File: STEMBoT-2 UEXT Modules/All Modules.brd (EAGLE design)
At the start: 81.2 x 50.7 mm, 39 parts, among them IC3 8to3 Encoder, IC6 8to3 Encoder, U1 HC-SR04, U2 TESEO-LIV3F, U3 CYBLE-012011-00

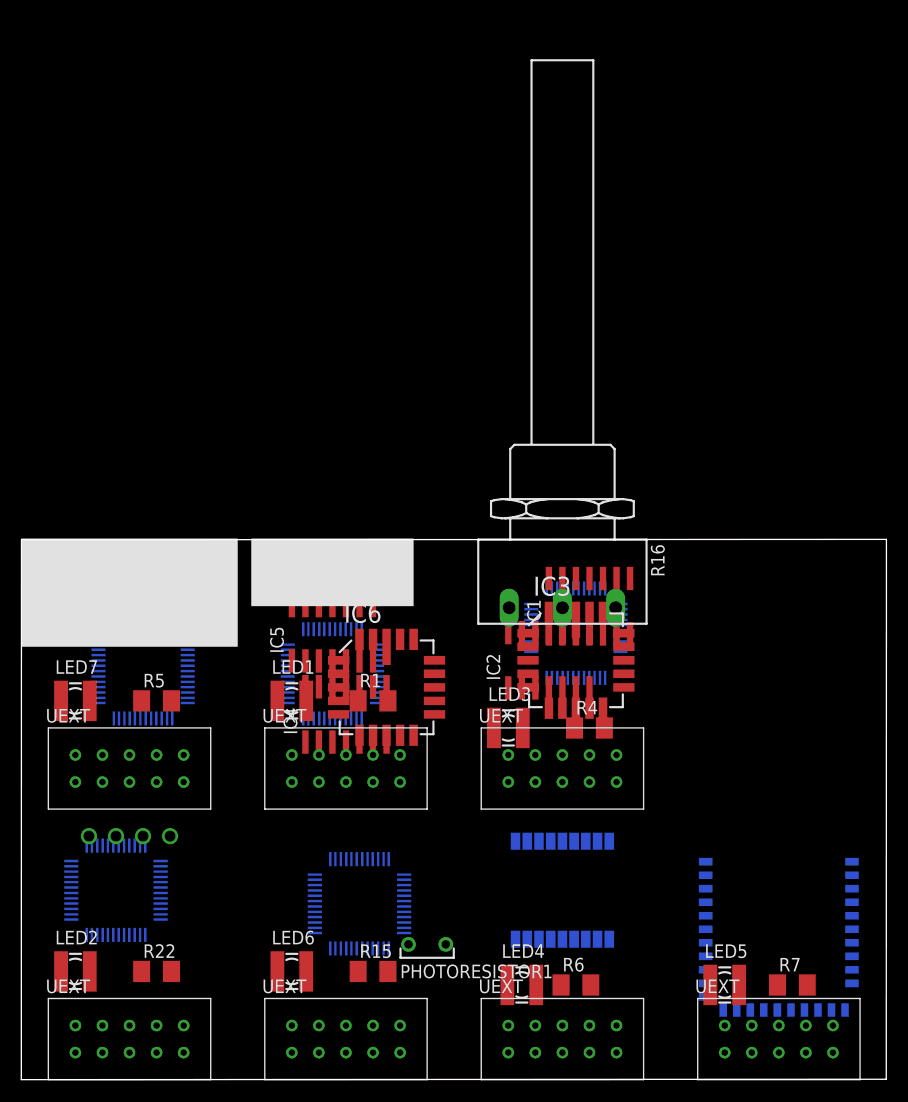
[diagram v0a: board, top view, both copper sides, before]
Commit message: changes to pcb with 6 mil traces
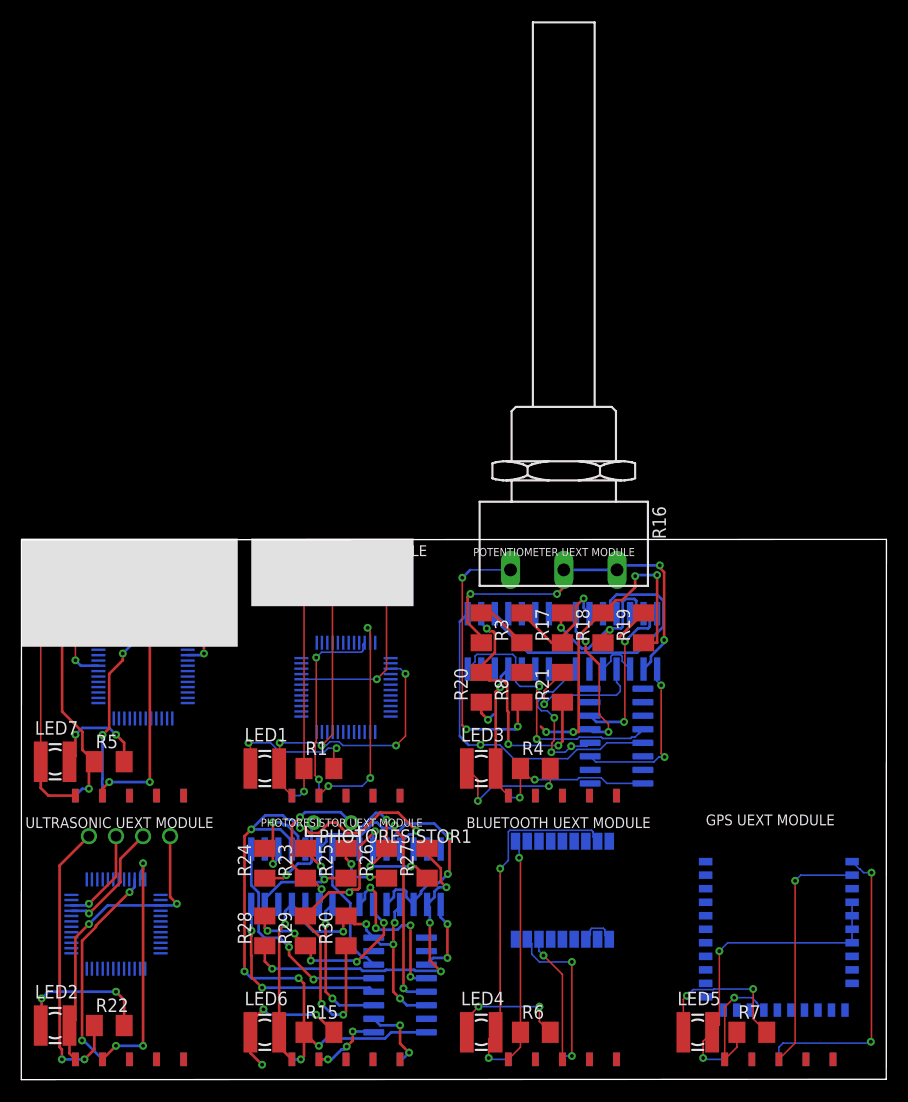
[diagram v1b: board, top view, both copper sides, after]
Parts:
- removed IC3, IC6: 8to3 Encoder, 74xx-eu:LCC20
- removed UX1, UX2, UX3, UX4, UX5, UX8, UX9: UEXT-CON, UEXT-Connecotr:UEXT-CON
- added R17, R18, R19, R2, R20, R21, R23, R24, R25, R26, R27, R28, R29, R3, R30, R8: 10k, rcl:M1206
- added U$12, U$2, U$3, U$7, U$8: UEXT-SMD, UEXT-Connecotr:UEXT-SMD
- added U$13, U$14: PARALLEL2SERIAL, SOIC127P600X175-16N:SOIC127P600X175-16N
- U$5, U$9: value LPC11C24FBD48/301 -> UEXT-SMD; device QFP50P900X900X160-48N:QFP50P900X900X160-48N -> UEXT-Connecotr:UEXT-SMD
- moved U$5 44.6 mm to (10.2, 26.7), flipped to the top
- moved U$9 24.0 mm to (50.8, 1.91), flipped to the top
- moved IC5 23.7 mm to (35.6, 19.1), flipped to the bottom
- moved IC4 16.1 mm to (25.4, 19.1), flipped to the bottom
- moved PHOTORESISTOR1 14.5 mm to (29.2, 24.1)
- moved R1 8.13 mm to (27.9, 29.2)
- moved R15 7.65 mm to (27.9, 4.45)
- moved R5 7.24 mm to (8.26, 29.8)
- moved LED1 6.84 mm to (22.9, 29.2)
- moved R22 6.75 mm to (8.26, 5.08)
- moved R4 6.35 mm to (48.3, 29.2)
- moved LED6 6.25 mm to (22.9, 4.45)
- moved LED7 6.02 mm to (3.17, 29.8)
- moved LED4 5.85 mm to (43.2, 4.45)
- moved R6 5.85 mm to (48.3, 4.45)
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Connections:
- removed net GND: IC3.10, IC6.10
- removed net N$46: IC3.9, U$5.34
- removed net N$47: IC3.8, U$5.35
- removed net N$70: U$9.46, UX8.3
- removed net N$71: U$9.47, UX8.4
- removed net N$72: IC6.12, U$9.33
- removed net N$73: IC6.9, U$9.34
- removed net N$74: IC6.8, U$9.35
- removed net V+: IC1.4, IC2.4, IC4.4, IC5.4
- removed net V-: IC1.11, IC2.11, IC4.11, IC5.11
- removed net VCC: IC3.20, IC6.20
- new net N$18: PHOTORESISTOR1.1, R24.1
- new net N$20: R16.1E, R8.1
- net N$1: now also U$8.1; no longer UX2.1
- net N$10: now also IC1.4, IC2.4, R21.2, U$13.16, U$13.6, U$2.2; no longer IC3.5, IC3.7, U$5.21, U$5.3, UX1.2
- net N$11: now also U$13.10, U$2.9; no longer U$5.47, UX1.4
- net N$12: now also U$14.9, U$3.4; no longer IC3.12, U$5.33
- net N$14: now also U$5.2; no longer UX3.2
- net N$15: now also U$5.3; no longer UX3.3
- net N$16: now also U$5.4; no longer UX3.4
- net N$19: now also U$14.10, U$3.9; no longer U$9.3
- net N$21: now also U$9.2; no longer UX5.2
- net N$22: now also U$9.1; no longer UX5.1
- net N$23: now also U$9.5; no longer UX5.5
- net N$24: now also U$9.6; no longer UX5.6
- net N$26: now also U$12.1; no longer UX4.1
- net N$27: now also U$12.6; no longer UX4.6
- net N$28: now also U$12.5; no longer UX4.5
- net N$29: now also U$12.2; no longer UX4.2
- net N$3: now also U$8.2; no longer UX2.2
- net N$33: now also R2.2, R3.1
- net N$34: now also R17.1, R3.2
- net N$35: now also R17.2, R18.1
- net N$36: now also R18.2, R19.1
- net N$37: now also R19.2, R20.1
- net N$38: now also R20.2, R21.1
- net N$39: now also U$13.11; no longer IC3.13
- net N$4: now also U$8.3; no longer UX2.3
- net N$40: now also U$13.12; no longer IC3.14
- net N$41: now also U$13.13; no longer IC3.15
- net N$42: now also U$13.14; no longer IC3.17
- net N$43: now also U$13.3; no longer IC3.2
- net N$44: now also U$13.4; no longer IC3.3
- net N$45: now also U$13.5; no longer IC3.4
- net N$48: now also R8.2; no longer R16.1E
- net N$49: now also R25.2, R26.1
- net N$5: now also U$8.4; no longer UX2.4
- net N$50: now also R2.1
- net N$52: now also IC1.11, IC2.11, U$13.8, U$2.1; no longer U$5.20, UX1.1
- net N$54: now also R26.2, R27.1
- net N$55: now also R27.2, R28.1
- net N$56: now also R28.2, R29.1
- net N$57: now also R29.2, R30.1
- net N$58: now also U$14.11; no longer IC6.13
- net N$59: now also U$14.12; no longer IC6.14
- net N$60: now also U$14.13; no longer IC6.15
- net N$61: now also U$14.14; no longer IC6.17
- net N$62: now also U$14.3; no longer IC6.2
- net N$63: now also U$14.4; no longer IC6.3
- net N$64: now also U$14.5; no longer IC6.4
- net N$65: now also R24.2; no longer PHOTORESISTOR1.1
- net N$66: now also IC4.11, IC5.11, U$14.8, U$3.1; no longer U$9.20, UX8.1
- net N$68: now also R23.1
- net N$69: now also IC4.4, IC5.4, R30.2, U$14.16, U$14.6, U$3.2; no longer IC6.5, IC6.7, U$9.21, UX8.2
- net N$7: now also U$5.1; no longer UX3.1
- net N$8: now also U$13.9, U$2.4; no longer U$5.46, UX1.3
- net N$81: now also U$7.1; no longer UX9.1
- net N$84: now also U$7.2; no longer UX9.2
- net N$85: now also U$7.3; no longer UX9.3
- net N$86: now also U$7.4; no longer UX9.4
- net N$9: now also R23.2, R25.1
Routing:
- net N$66: track 0.00 -> 66.9 mm, vias 0 -> 7
- net N$69: track 0.00 -> 41.7 mm, vias 0 -> 6
- net N$3: track 0.00 -> 41.5 mm, vias 0 -> 4
- net N$14: track 0.00 -> 38.6 mm, vias 0 -> 3
- net N$50: track 0.00 -> 35.8 mm, vias 0 -> 4
- net N$22: track 0.00 -> 33.0 mm, vias 0 -> 2
- net N$55: track 0.00 -> 32.5 mm, vias 0 -> 4
- net N$48: track 0.00 -> 32.2 mm
- net N$57: track 0.00 -> 31.7 mm, vias 0 -> 4
- net N$65: track 0.00 -> 30.8 mm, vias 0 -> 4
- net N$36: track 0.00 -> 30.8 mm, vias 0 -> 4
- net N$45: track 0.00 -> 30.5 mm, vias 0 -> 1
- net N$26: track 0.00 -> 29.3 mm, vias 0 -> 2
- net N$84: track 0.00 -> 29.3 mm, vias 0 -> 2
- net N$28: track 0.00 -> 28.1 mm, vias 0 -> 2
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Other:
- board text added: "BLUETOOTH UEXT MODULE"
- board text added: "GPS UEXT MODULE"
- board text added: "IR REMOTE UEXT MODULE"
- board text added: "IR SESNOR UEXT MODULE"
- board text added: "PHOTORESISTOR UEXT MODULE"
- board text added: "POTENTIOMETER UEXT MODULE"
- board text added: "ULTRASONIC UEXT MODULE"

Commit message: added board file and new switch library
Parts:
- removed IC4, IC5: (no value), linear:SO14
- removed PHOTORESISTOR1: M9960_11A, photo-elements:M9960
- added C1, C10, C2, C3, C4, C5, C6, C7, C8, C9: CAPACITORS-0603, CAPACITORS:C0603
- added D1, D3: SFH482, led:SFH482
- added D2, D4: BP104, opto-trans-siemens:BP104
- added DZ1, DZ2: LZR182, led:LZR182
- added IC3: 74HC165PW,118, 74HC165PW_118:SOP65P640X110-16N
- added J1, J2, J3, J4, J5, J6: FTSH-105-01-XXX-DV-K, FTSH-105-01-XXX-DV-K:FTSH-105-01-XXX-DV-K
- added LED8: LSG-T676, led:P-LCC4-0
- added PH1, PH2: VT20N1, photo-elements:TO46-VT200
- added Q1: MMBT3904LP-7, NPN BJT:DFN101X61X53-3N
- added Q2, Q3: MMBT3904LP-7, MMBT3904LP-7:DFN101X61X53-3N
- added R10, R11, R12, R13, R14, R31, R32, R33, R34, R35, R36, R37, R38, R39, R40, R41, R42, R49, R50, R51, R55, R61, R9: ERJ-1RHD3601C, Resistor:RESC0603X26N
- added R43, R44, R45, R46, R47, R48, R52, R53, R57, R58: 1k, rcl:M1206
- added R54: PC16S, piher:PC16S
- added S1, S2, S3, S4, S5, S6: 2-1437565-7, 2-1437565-7 (tactile switch):SW_2-1437565-7
- added U$15: UEXT-SMD, UEXT-Connecotr:UEXT-SMD
- added U10, U4, U7: SN74HC148D, SN74HC148D:SOIC127P600X175-16N
- added U11, U12, U5, U6, U8, U9: MAX964ESET, MAX964ESET:SOIC127P600X175-16N
- added U13: HC-SR04, HC-SR04:XCVR_HC-SR04
- added VR1, VR2: PVG3A200C01R00, TrimmerPot:TRIM_PVG3A200C01R00
- IC1, IC2: value (none) -> 74HC165PW,118; device linear:SO14 -> 74HC165PW_118:SOP65P640X110-16N
- R1, R15, R4, R5: value 1k -> ERJ-1RHD3601C; device rcl:M1206 -> Resistor:RESC0603X26N
- R16: value 1K ohm -> ERJ-1RHD3601C; device piher:PC16S -> Resistor:RESC0603X26N
- R17, R18, R19, R2, R21, R23, R24, R25, R26, R27, R28, R29, R3, R30, R8: value 10k -> ERJ-1RHD3601C; device rcl:M1206 -> Resistor:RESC0603X26N
- R20: value 10k -> PC16S; device rcl:M1206 -> piher:PC16S
- U$1, U$10: value LPC11C24FBD48/301 -> UEXT-SMD; device QFP50P900X900X160-48N:QFP50P900X900X160-48N -> UEXT-Connecotr:UEXT-SMD
- U$11: value CHQ1838 -> LPC11C24FBD48/301; device IRSensors:CHQ1838 -> QFP50P900X900X160-48N:QFP50P900X900X160-48N
- U$13: value PARALLEL2SERIAL -> UEXT-SMD; device SOIC127P600X175-16N:SOIC127P600X175-16N -> UEXT-Connecotr:UEXT-SMD
- U$14: value PARALLEL2SERIAL -> LPC11C24FBD48/301; device SOIC127P600X175-16N:SOIC127P600X175-16N -> QFP50P900X900X160-48N:QFP50P900X900X160-48N
- U$4: value HW740 -> LPC11C24FBD48/301; device IRSensors:HW740 -> QFP50P900X900X160-48N:QFP50P900X900X160-48N
- U$7: value UEXT-SMD -> LPC11C24FBD48/301; device UEXT-Connecotr:UEXT-SMD -> QFP50P900X900X160-48N:QFP50P900X900X160-48N
- U1: value HC-SR04 -> TSL260R-LF; device HC-SR04:XCVR_HC-SR04 -> TSL260R-LF:XDCR_TSL260R-LF
- moved R4 718.5 mm to (-334.0, 637.5)
- moved R8 718.2 mm to (-346.7, 637.5), turned to 0 degrees
- moved R3 703.2 mm to (-327.7, 637.5), turned to 0 degrees
- moved R5 700.6 mm to (-340.4, 637.5)
- moved R1 698.3 mm to (-315.0, 637.5)
- moved R2 697.9 mm to (-321.3, 637.5), turned to 0 degrees
- moved R7 691.1 mm to (-205.7, 638.8)
- moved IC2 684.0 mm to (-287.0, 638.8), flipped to the top
- moved IC1 681.6 mm to (-271.8, 638.8), flipped to the top
- moved R6 681.5 mm to (-200.7, 638.8)
- moved R22 670.5 mm to (-210.8, 638.8)
- moved LED5 657.4 mm to (-104.1, 640.1)
- moved R30 651.2 mm to (-119.4, 647.7), turned to 0 degrees
- moved LED6 650.5 mm to (-115.6, 640.1)
- moved U1 650.2 mm to (-194.3, 640.1), flipped to the top, turned to 0 degrees
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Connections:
- removed net GND_RF: U2.10, U2.12
- removed net N$3 (its old number): LED1.A, U$11.P$2, U$6.3, U$8.2
- removed net VCC_IO: U2.7
- removed net VCC_RF: U2.14
- removed net VDDR: U3.29
- new net N$100: U4.1, U6.15
- new net N$101: U4.12, U6.14
- new net N$102: U4.11, U6.11
- new net N$103: U4.10, U6.10
- new net N$104: U10.10, U12.10
- new net N$105: R1.2, R42.1, U11.1
- new net N$106: IC2.15, U$2.10
- new net N$107: IC2.2, U$2.9
- new net N$108: IC2.16, R20.1E, R30.2, R40.1, R42.2, U$2.1, U10.16, U11.12, U11.13
- new net N$109: R20.1S, U11.2, U11.4, U11.6, U11.8, U12.2, U12.4, U12.6, U12.8
- new net N$110: LED6.C, R52.2
- new net N$111: LED1.C, R43.2
- new net N$112: J1.10, R45.1, S1.3, U$7.3
- new net N$113: C1.2, C2.2, J1.1, LED2.A, R45.2, U$10.1, U$7.17, U$7.20, U$7.44, U$7.8, U13.1
- new net N$114: J4.10, R48.2, S4.1, U3.1
- new net N$115: LED3.C, R46.2
- new net N$116: U$11.16, U$13.6
- new net N$117: U$4.16, U$5.6
- new net N$118: U$4.15, U$5.5
- new net N$119: C3.2, C4.2, J2.1, LED3.A, R47.2, U$4.17, U$4.20, U$4.44, U$4.8, U$5.1, U1.2
- new net N$120: J2.4, U$4.29
- new net N$121: U$6.16, U$8.6
- new net N$122: J2.2, U$4.39
- new net N$123: J2.6, U$4.28
- new net N$124: U$6.15, U$8.5
- new net N$125: U$4.12
- new net N$126: J4.2, U3.24
- new net N$127: J2.10, R47.1, S2.3, U$4.3
- new net N$128: J4.4, U3.23
- new net N$129: J3.4, U$6.29
- new net N$130: J3.2, U$6.39
- new net N$131: J3.6, U$6.28
- new net N$132: D3.K, R49.2
- new net N$133: D4.A, R50.2
- new net N$134: R51.1, VR2.2
- new net N$135: J3.10, R44.1, S3.3, U$6.3
- new net N$136: R51.2, U$6.32
- new net N$137: C5.1, C6.1, J3.3, J3.5, J3.9, R43.1, R49.1, R50.1, S3.2, U$6.21, U$6.41, U$6.5, U$8.2, VR2.1
- new net N$138: C5.2, C6.2, D3.A, D4.K, J3.1, LED1.A, R44.2, U$6.17, U$6.20, U$6.44, U$6.8, U$8.1, VR2.3
- new net N$139: U$11.15, U$13.5
- new net N$140: J5.4, U$11.29
- new net N$141: J5.2, U$11.39
- new net N$142: J5.6, U$11.28
- new net N$143: J5.10, R53.1, S5.3, U$11.3
- new net N$144: C7.1, C8.1, J5.3, J5.5, J5.9, R52.1, R54.1A, S5.2, U$11.21, U$11.41, U$11.5, U$13.2
- new net N$145: IC2.1, U$2.8
- new net N$146: R54.1S
- new net N$147: U$11.32
- new net N$148: C10.2, C9.2, J6.1, LED7.A, PH2.1, R58.2, U$14.17, U$14.20, U$14.44, U$14.8, U$15.1
- new net N$149: C7.2, C8.2, J5.1, LED6.A, R53.2, R54.1E, U$11.17, U$11.20, U$11.44, U$11.8, U$13.1
- new net N$150: LED7.C, R57.2
- new net N$151: U$14.16, U$15.6
- new net N$152: U$14.15, U$15.5
- new net N$153: J6.4, U$14.29
- new net N$154: J6.2, U$14.39
- new net N$155: J6.6, U$14.28
- new net N$156: J6.10, R58.1, S6.3, U$14.3
- new net N$157: PH2.2, R55.1
- new net N$159: R61.1
- new net N$160: R61.2, U$14.32
- new net N$161: C10.1, C9.1, J6.3, J6.5, J6.9, R55.2, R57.1, S6.2, U$14.21, U$14.41, U$14.5, U$15.2
- new net N$162: IC1.1, U$3.8
- new net N$163: IC3.1, U$1.8
- new net N$31: D1.K, R9.2
- new net N$32: LED8.2, R11.2
- new net N$46: LED8.4, R12.1
- new net N$47: LED8.3, Q1.3
- new net N$51: IC1.16, PH1.1, R23.1, R3.2, R8.2, U$3.1, U7.16, U8.12, U8.13
- new net N$70: D2.A, R10.2
- new net N$71: R14.1, VR1.2
- new net N$72: Q1.1, R13.1
- new net N$73: U10.12, U12.14
- new net N$74: IC3.11, U4.9
- new net N$75: IC3.12, U4.7
- new net N$76: IC3.13, U4.6
- new net N$77: IC3.9, R13.2, U$1.7
- new net N$78: U10.11, U12.11
- new net N$79: R14.2, U5.2, U5.4, U5.6, U5.8, U6.2, U6.4, U6.6, U6.8
- new net N$80: R34.1, R39.2, U5.1
- new net N$82: U$10.5, U$7.15
- new net N$83: R32.1, R34.2, U5.3
- new net N$89: R32.2, R35.1, U5.5
- new net N$91: R31.1, R35.2, U5.7
- new net N$92: R31.2, R36.2, U6.1
- new net N$93: R33.2, R36.1, U6.3
- new net N$94: R33.1, R37.2, U6.5
- new net N$95: R37.1, R38.2, U6.7
- new net N$96: U4.4, U5.15
- new net N$97: U4.3, U5.14
- new net N$98: U4.2, U5.11
- new net N$99: U4.13, U5.10
- new net VCC: U12.13, U9.13
- net N$1: now also C1.1, C2.1, J1.3, J1.5, J1.9, R22.1, S1.2, U$10.2, U$7.21, U$7.41, U$7.5, U13.4; no longer R1.1, U$11.P$1, U$8.1
- net N$10: now also DZ1.K2, Q2.3; no longer IC1.4, IC2.4, LED3.A, R21.2, U$13.16, U$13.6, U$2.2
- net N$11: now also IC1.13, U7.6; no longer U$13.10, U$2.9
- net N$12: now also PH1.2, R5.1, U8.2, U8.4, U8.6, U8.8, U9.2, U9.4, U9.6, U9.8; no longer U$14.9, U$3.4
- net N$13: now also IC1.15, U$3.10; no longer LED7.A, R5.2
- net N$14: now also IC3.2, U$1.9; no longer LED7.C, U$1.3, U$4.P$2, U$5.2
- net N$15: now also DZ2.K2, Q3.3; no longer U$1.46, U$5.3
- net N$16: now also IC1.9, R4.1, U$3.7; no longer U$1.47, U$5.4
- net N$17: now also IC2.11, U10.9; no longer U$1.32, U$4.P$3
- net N$18: now also DZ1.A2, R23.2; no longer PHOTORESISTOR1.1, R24.1
- net N$19: now also IC1.11, U7.9; no longer U$14.10, U$3.9
- net N$2: now also U1.3; no longer LED1.C, R1.2
- net N$20: now also IC1.10, IC1.12, U7.7; no longer R16.1E, R8.1
- net N$21: now also U2.10, U2.12
- net N$22: now also U2.14, U2.7
- net N$26: now also J4.1, R48.1, U3.10, U3.15, U3.29; no longer U3.25, U3.26, U3.27, U3.28
- net N$29: now also J4.3, J4.5, J4.9, S4.3, U3.25, U3.26, U3.27, U3.28; no longer U3.15
- net N$33: now also R15.1, R2.1, U8.3; no longer IC1.6, R2.2, R3.1
- net N$34: now also R15.2, R16.2, U8.5; no longer IC1.9, R17.1, R3.2
- net N$35: now also R16.1, U8.7; no longer IC1.13, R18.1
- net N$36: now also R17.1, R21.2, U9.1; no longer IC2.2, R18.2, R19.1
- net N$37: now also R18.1, R21.1, U9.3; no longer IC2.6, R19.2, R20.1
- net N$38: now also R18.2, R19.2, U9.5; no longer IC2.9, R20.2, R21.1
- net N$39: now also DZ1.K1, IC1.8, Q2.2, R19.1, R5.2, U$3.2, U7.5, U7.8, U9.12, U9.7; no longer IC1.1, U$13.11
- net N$4: now also Q3.1, R41.2; no longer U$6.46, U$8.3
- net N$40: now also U7.4, U8.15; no longer IC1.7, U$13.12
- net N$41: now also U7.3, U8.14; no longer IC1.8, U$13.13
- net N$42: now also U7.2, U8.11; no longer IC1.14, U$13.14
- net N$43: now also U7.13, U8.10; no longer IC2.1, U$13.3
- net N$44: now also U7.1, U9.15; no longer IC2.7, U$13.4
- net N$45: now also U7.12, U9.14; no longer IC2.8, U$13.5
- net N$48: now also U7.11, U9.11; no longer IC1.10, IC1.12, IC1.3, IC1.5, IC2.10, IC2.3, IC2.5, R8.2
- net N$49: now also U7.10, U9.10; no longer IC4.9, R25.2, R26.1
- net N$5: now also DZ2.A1, R30.1; no longer U$6.47, U$8.4
- net N$50: now also R2.2, R8.1, U8.1; no longer IC1.2, R16.1A, R16.1S, R2.1
- net N$52: now also IC1.2, U$3.9; no longer IC1.11, IC2.11, R4.1, U$13.8, U$2.1
- net N$53: now also IC2.10, IC2.12, U10.7; no longer LED3.C, R4.2
- net N$54: now also IC2.13, U10.6; no longer IC4.13, R26.2, R27.1
- net N$55: now also D1.A, D2.K, IC3.14, IC3.16, IC3.3, IC3.4, IC3.5, IC3.6, IC3.8, LED8.1, Q1.2, R10.1, R11.1, R12.2, R38.1, R39.1, R9.1, U$1.1, U$1.2, U4.16, U4.5, U4.8, U5.12, U5.13, U6.12, U6.13, VR1.1, VR1.3; no longer IC5.2, R27.2, R28.1
- net N$56: now also IC2.9, R41.1, U$2.7; no longer IC5.6, R28.2, R29.1
- net N$57: now also DZ2.A2, R40.2; no longer IC5.9, R29.2, R30.1
- net N$58: now also R1.1, R24.1, U11.3; no longer IC4.1, U$14.11
- net N$59: now also R24.2, R25.2, U11.5; no longer IC4.7, U$14.12
- net N$6: now also C3.1, C4.1, J2.3, J2.5, J2.9, R46.1, S2.2, U$4.21, U$4.41, U$4.5, U$5.2, U1.1; no longer U$11.P$3, U$6.32
- net N$60: now also R25.1, R26.2, U11.7; no longer IC4.8, U$14.13
- net N$61: now also R26.1, R29.2, U12.1; no longer IC4.14, U$14.14
- net N$62: now also R27.1, R29.1, U12.3; no longer IC5.1, U$14.3
- net N$63: now also R27.2, R28.2, U12.5; no longer IC5.7, U$14.4
- net N$64: now also DZ2.K1, IC2.8, Q3.2, R20.1A, R28.1, U$2.2, U10.5, U10.8, U12.12, U12.7; no longer IC5.8, U$14.5
- net N$65: now also U10.4, U11.15; no longer IC4.10, IC4.12, IC4.3, IC4.5, IC5.10, IC5.3, IC5.5, R24.2
- net N$66: now also U10.3, U11.14; no longer IC4.11, IC5.11, R15.1, U$14.8, U$3.1
- net N$67: now also U10.2, U11.11; no longer LED6.C, R15.2
- net N$68: now also U10.13, U11.10; no longer IC4.2, PHOTORESISTOR1.2, R23.1
- net N$69: now also U10.1, U12.15; no longer IC4.4, IC5.4, LED6.A, R30.2, U$14.16, U$14.6, U$3.2
- net N$7: now also IC3.15, U$1.10; no longer R5.1, U$4.P$1, U$5.1
- net N$8: now also Q2.1, R4.2; no longer U$13.9, U$2.4
- net N$81: now also U$10.6, U$7.16; no longer R22.1, U$7.1, U1.1
- net N$84: now also J1.4, U$7.29; no longer LED2.A, U$10.3, U$7.2, U1.4
- net N$85: now also J1.2, U$7.39; no longer U$10.46, U$7.3
- net N$86: now also J1.6, U$7.28; no longer U$10.47, U$7.4
- net N$87: now also U$7.12, U13.2; no longer U$10.33, U1.3
- net N$88: now also U$7.11, U13.3; no longer U$10.34, U1.2
- net N$9: now also DZ1.A1, R3.1; no longer IC4.6, R23.2, R25.1
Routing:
- net N$66: track 66.9 -> 0.00 mm, vias 7 -> 0
- net N$69: track 41.7 -> 0.00 mm, vias 6 -> 0
- net N$3 (its old number): track 41.5 -> 0.00 mm, vias 4 -> 0
- net N$14: track 38.6 -> 0.00 mm, vias 3 -> 0
- net N$50: track 35.8 -> 0.00 mm, vias 4 -> 0
- net N$22: track 33.0 -> 0.00 mm, vias 2 -> 0
- net N$55: track 32.5 -> 0.00 mm, vias 4 -> 0
- net N$48: track 32.2 -> 0.00 mm
- net N$57: track 31.7 -> 0.00 mm, vias 4 -> 0
- net N$65: track 30.8 -> 0.00 mm, vias 4 -> 0
- net N$36: track 30.8 -> 0.00 mm, vias 4 -> 0
- net N$45: track 30.5 -> 0.00 mm, vias 1 -> 0
- net N$26: track 29.3 -> 0.00 mm, vias 2 -> 0
- net N$84: track 29.3 -> 0.00 mm, vias 2 -> 0
- net N$28: track 28.1 -> 0.00 mm, vias 2 -> 0
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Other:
- board size 81.2 x 50.7 mm -> 160 x 100 mm
- board text removed: "BLUETOOTH UEXT MODULE"
- board text removed: "GPS UEXT MODULE"
- board text removed: "IR REMOTE UEXT MODULE"
- board text removed: "IR SESNOR UEXT MODULE"
- board text removed: "PHOTORESISTOR UEXT MODULE"
- board text removed: "POTENTIOMETER UEXT MODULE"
- board text removed: "ULTRASONIC UEXT MODULE"

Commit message: removed silk screens
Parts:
- removed S4: 2-1437565-7, 2-1437565-7 (tactile switch):SW_2-1437565-7
- added S7: B3U-1000P, B3U-1000P:SW_B3U-1000P
- R20, R54: value PC16S -> PC16S(NOSILK); device piher:PC16S -> piher:PC16S(NOSILK)
- S1, S2, S3, S5, S6: value 2-1437565-7 -> B3U-1000P; device 2-1437565-7 (tactile switch):SW_2-1437565-7 -> B3U-1000P:SW_B3U-1000P
- U13: value HC-SR04 -> HC-SR04(NOSILK); device HC-SR04:XCVR_HC-SR04 -> HC-SR04:XCVR_HC-SR04(NOSILK)
- moved R11 773.7 mm to (115.6, 31.8), flipped to the bottom
- moved R10 768.2 mm to (113.0, 31.8), flipped to the bottom
- moved R9 762.8 mm to (110.5, 31.8), flipped to the bottom
- moved D1 746.7 mm to (110.5, 48.3)
- moved R8 745.6 mm to (91.4, 34.3), flipped to the bottom
- moved R5 743.3 mm to (94.0, 34.3), flipped to the bottom
- moved R4 741.1 mm to (96.5, 34.3), flipped to the bottom
- moved R3 739.7 mm to (100.3, 34.3), flipped to the bottom
- moved R2 738.2 mm to (104.1, 34.3), flipped to the bottom
- moved IC3 737.7 mm to (116.8, 31.8)
- moved R1 724.4 mm to (121.9, 59.7), flipped to the bottom
- moved Q1 710.6 mm to (123.2, 31.8), flipped to the bottom
- moved IC1 707.9 mm to (96.5, 34.3)
- moved IC2 706.0 mm to (116.8, 59.7)
- moved Q2 693.7 mm to (88.9, 34.3), flipped to the bottom
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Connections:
- net N$1: now also S6.1; no longer S1.2
- net N$112: now also S6.2; no longer S1.3
- net N$114: now also S2.1; no longer S4.1
- net N$127: now also S1.2; no longer S2.3
- net N$135: now also S7.2; no longer S3.3
- net N$137: now also S7.1; no longer S3.2
- net N$143: now also S3.2; no longer S5.3
- net N$144: now also S3.1; no longer S5.2
- net N$156: now also S5.2; no longer S6.3
- net N$161: now also S5.1; no longer S6.2
- net N$29: now also S2.2; no longer S4.3
- net N$6: now also S1.1; no longer S2.2

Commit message: changes to board and schematic
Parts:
- moved VR1 17.6 mm to (116.3, 48.0)
- moved PH1 17.5 mm to (97.3, 47.8)
- moved D4 17.5 mm to (82.5, 47.5)
- moved C5 17.3 mm to (75.4, 31.5)
- moved C6 17.3 mm to (72.9, 31.5)
- moved DZ1 14.8 mm to (89.4, 31.5)
- moved Q3 10.4 mm to (109.2, 52.6)
- moved VR2 6.62 mm to (75.9, 47.5)
- moved D3 6.12 mm to (70.1, 47.5)
- moved IC1 2.54 mm to (96.5, 31.8)
- moved Q2 2.54 mm to (88.9, 31.8)
- moved R15 2.54 mm to (104.1, 34.3)
- moved R16 2.54 mm to (101.6, 34.3)
- moved R17 2.54 mm to (99.1, 34.3)
- moved R18 2.54 mm to (91.4, 34.3)
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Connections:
- removed net VCC: U12.13, U9.13
- net N$108: now also U12.13
- net N$51: now also U9.13
